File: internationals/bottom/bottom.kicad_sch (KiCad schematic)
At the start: 42 parts, among them J1 JST-XH-B6B, J2 Header-01x09, J4 JST-XH-B4B, U1 ESP-S2-Pico, U2 MINI560 3.3V

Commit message: pcbs: bottom: feat: add spare 3.3V JSTs to schematics
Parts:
- added J3, J5, J6, J7: 3.3V-JST-XH-B2B, Connector_JST:JST_XH_B2B-XH-A_1x02_P2.50mm_Vertical, symbol Connector:Conn_01x02_Pin
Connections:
- net +3.3V: now also J3.2 (Pin_2), J5.2 (Pin_2), J6.2 (Pin_2), J7.2 (Pin_2)
- net GND: now also J3.1 (Pin_1), J5.1 (Pin_1), J6.1 (Pin_1), J7.1 (Pin_1)

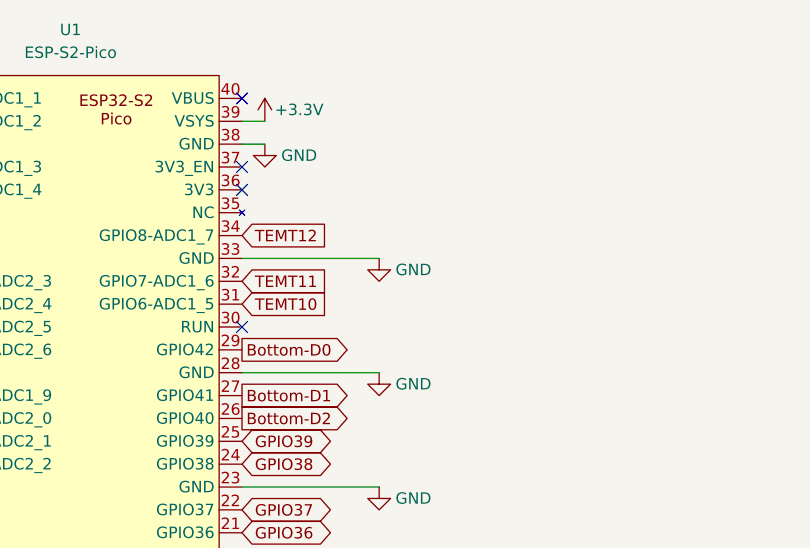
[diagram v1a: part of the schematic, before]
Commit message: pcbs: bottom: feat: add pull-up resistor for RUN
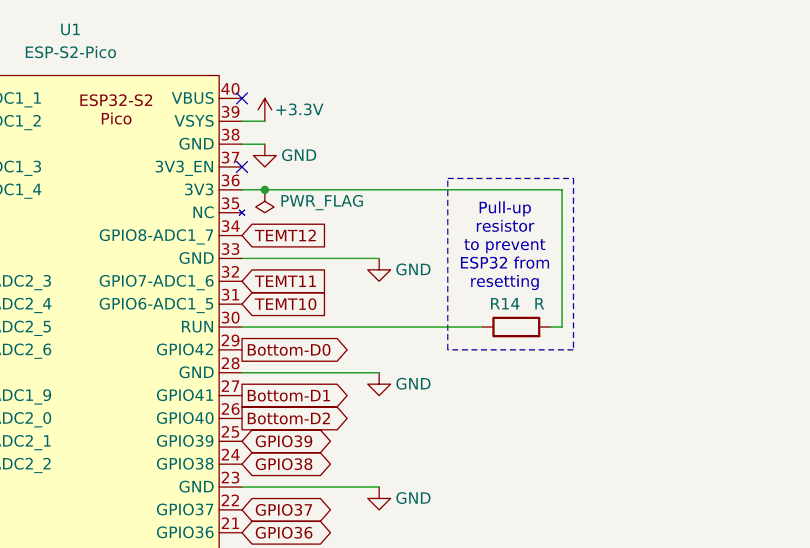
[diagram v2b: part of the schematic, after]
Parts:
- added R14: R, PCM_Resistor_THT_AKL:R_Axial_DIN0204_L3.6mm_D1.6mm_P5.08mm_Horizontal, symbol Device:R
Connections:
- net at U1.30 (RUN): now also R14.1
- net at U1.36 (3V3): now also R14.2
- no-connect marks 5 -> 3
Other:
- note added: "Pull-up resistor to prevent ESP32 from resetting"
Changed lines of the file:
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@@
 		(title "Bottom Plate")
 		(date "2024-06-08")
-		(rev "1.3.0")
+		(rev "1.4.0")
 		(company "Zhou Yikun & Zachary Ang")
 		(comment 1 "RoboCup Junior Soccer Open 2024")
@@
 	)
 	(junction
+		(at 157.48 31.75)
+		(diameter 0)
+		(color 0 0 0 0)
+	)
+	(junction
 		(at 53.34 151.13)
 		(diameter 0)
@@
 	)
 	(no_connect
-		(at 154.94 31.75)
-	)
-	(no_connect
 		(at 254 101.6)
 	)
@@
 		(at 154.94 21.59)
 	)
-	(no_connect
-		(at 154.94 46.99)
-	)
 	(wire
 		(pts
@@
 	(wire
 		(pts
+			(xy 154.94 31.75) (xy 157.48 31.75)
+		)
+		(stroke
+			(width 0)
+			(type default)
+		)
+	)
+	(wire
+		(pts
 			(xy 40.64 110.49) (xy 43.18 110.49)
 		)
@@
 	(wire
 		(pts
+			(xy 157.48 31.75) (xy 190.5 31.75)
+		)
+		(stroke
+			(width 0)
+			(type default)
+		)
+	)
+	(wire
+		(pts
 			(xy 266.7 163.83) (xy 269.24 163.83)
 		)
@@
 	(wire
 		(pts
+			(xy 154.94 46.99) (xy 181.61 46.99)
+		)
+		(stroke
+			(width 0)
+			(type default)
+		)
+	)
+	(wire
+		(pts
 			(xy 40.64 135.89) (xy 43.18 135.89)
 		)
@@
 	(wire
 		(pts
+			(xy 190.5 46.99) (xy 189.23 46.99)
+		)
+		(stroke
+			(width 0)
+			(type default)
+		)
+	)
+	(wire
+		(pts
 			(xy 53.34 146.05) (xy 53.34 151.13)
 		)
@@
 	(wire
 		(pts
+			(xy 190.5 31.75) (xy 190.5 46.99)
+		)
+		(stroke
+			(width 0)
+			(type default)
+		)
+	)
+	(wire
+		(pts
 			(xy 254 54.61) (xy 269.24 54.61)
 		)
@@
 	)
 	(rectangle
+		(start 177.8 30.48)
+		(end 191.77 49.53)
+		(stroke
+			(width 0)
+			(type dash)
+		)
+		(fill
+			(type none)
+		)
+	)
+	(rectangle
 		(start 241.3 12.7)
 		(end 284.48 44.45)
@@
 		)
 	)
+	(text "Pull-up\nresistor\nto prevent\nESP32 from\nresetting"
+		(exclude_from_sim no)
+		(at 184.15 38.1 0)
+		(effects
+			(font
+				(size 1.27 1.27)
+			)
+		)
+	)
 	(global_label "Bottom-D2"
 		(shape input)
@@
 	)
 	(symbol
+		(lib_id "power:PWR_FLAG")
+		(at 157.48 31.75 180)
+		(unit 1)
+		(exclude_from_sim no)
+		(in_bom yes)
+		(on_board yes)
+		(dnp no)
+		(property "Reference" "#FLG03"
+			(at 157.48 33.655 0)
+			(effects
+				(font
+					(size 1.27 1.27)
+				)
+				(hide yes)
+			)
+		)
+		(property "Value" "PWR_FLAG"
+			(at 163.83 33.02 0)
+			(effects
+				(font
+					(size 1.27 1.27)
+				)
+			)
+		)
+		(property "Footprint" ""
+			(at 157.48 31.75 0)
+			(effects
+				(font
+					(size 1.27 1.27)
+				)
+				(hide yes)
+			)
+		)
+		(property "Datasheet" "~"
+			(at 157.48 31.75 0)
+			(effects
+				(font
+					(size 1.27 1.27)
+				)
+				(hide yes)
+			)
+		)
+		(property "Description" "Special symbol for telling ERC where power comes from"
+			(at 157.48 31.75 0)
+			(effects
+				(font
+					(size 1.27 1.27)
+				)
+				(hide yes)
+			)
+		)
+		(pin "1"
+		)
+		(instances
+			(project "bottom"
+				(path "/0df53960-77ed-48ae-9914-15d62b01c54c"
+					(reference "#FLG03")
+					(unit 1)
+				)
+			)
+		)
+	)
+	(symbol
 		(lib_id "Device:R_Photo")
 		(at 69.85 22.86 0)
@@
 					(unit 1)
 				)
+			)
+		)
+	)
+	(symbol
+		(lib_id "Device:R")
+		(at 185.42 46.99 90)
+		(unit 1)
+		(exclude_from_sim no)
+		(in_bom yes)
+		(on_board yes)
+		(dnp no)
+		(property "Reference" "R14"
+			(at 184.15 44.45 90)
+			(effects
+				(font
+					(size 1.27 1.27)
+				)
+			)
+		)
+		(property "Value" "R"
+			(at 187.96 44.45 90)
+			(effects
+				(font
+					(size 1.27 1.27)
+				)
+			)
+		)
+		(property "Footprint" "PCM_Resistor_THT_AKL:R_Axial_DIN0204_L3.6mm_D1.6mm_P5.08mm_Horizontal"
+			(at 185.42 48.768 90)
+			(effects
+				(font
+					(size 1.27 1.27)
+				)
+				(hide yes)
+			)
+		)
+		(property "Datasheet" "~"
+			(at 185.42 46.99 0)
+			(effects
+				(font
+					(size 1.27 1.27)
+				)
+				(hide yes)
+			)
+		)
+		(property "Description" ""
+			(at 185.42 46.99 0)
+			(effects
+				(font
+					(size 1.27 1.27)
+				)
+				(hide yes)
+			)
+		)
+		(pin "2"
+		)
+		(pin "1"
+		)
+		(instances
+			(project "bottom"
+				(path "/0df53960-77ed-48ae-9914-15d62b01c54c"
+					(reference "R14")
+					(unit 1)
+				)

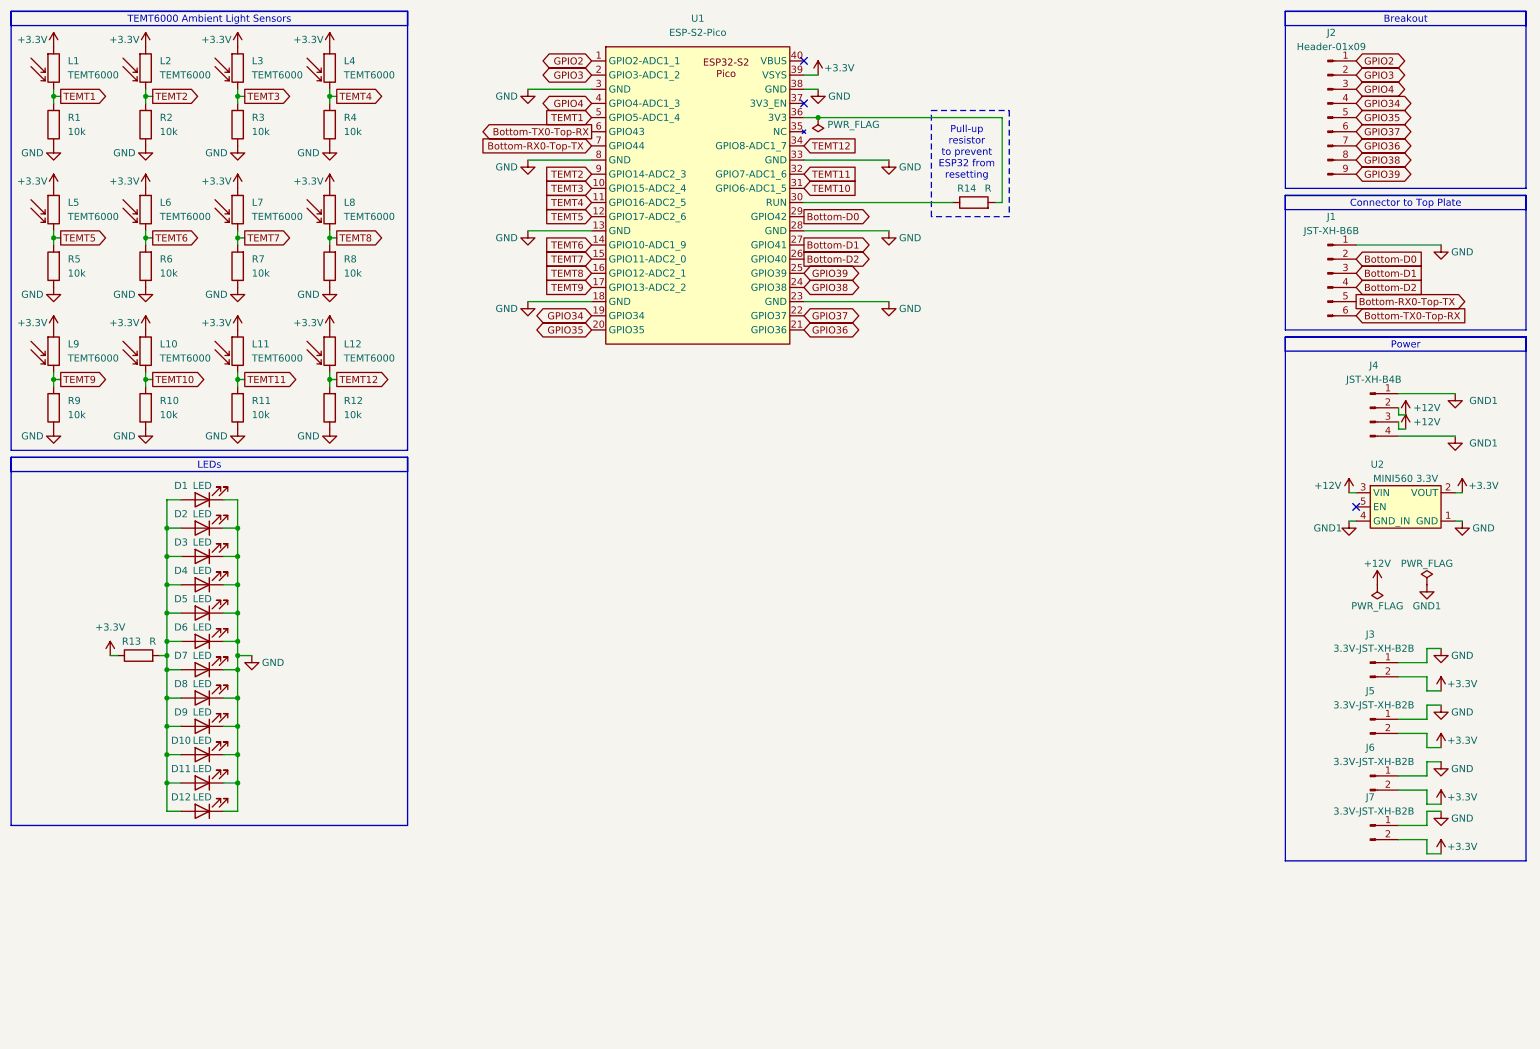
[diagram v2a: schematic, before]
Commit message: pcbs: bottom: feat: add mounting holes in schematics and swap labels
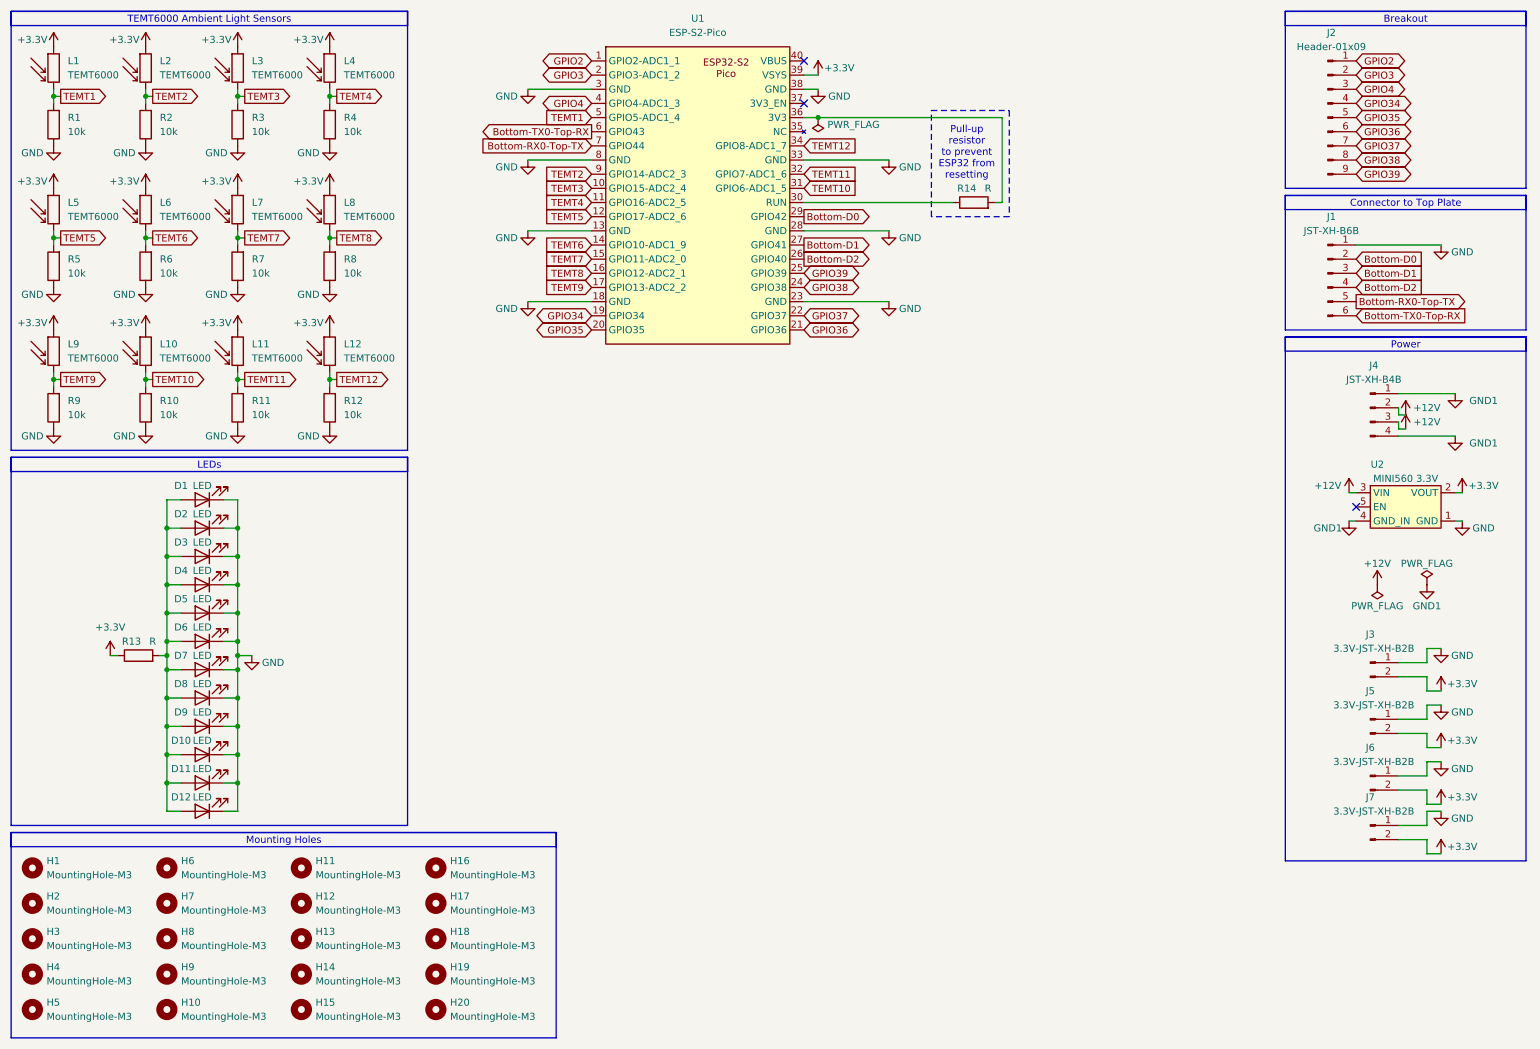
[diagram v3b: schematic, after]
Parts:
- added H1, H10, H11, H12, H13, H14, H15, H16, H17, H18, H19, H2, H20, H3, H4, H5, H6, H7, H8, H9: MountingHole-M3, MountingHole:MountingHole_3.2mm_M3_Pad_Via, symbol Mechanical:MountingHole
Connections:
- net GPIO36: now also J2.6 (Pin_6); no longer J2.7 (Pin_7)
- net GPIO37: now also J2.7 (Pin_7); no longer J2.6 (Pin_6)
